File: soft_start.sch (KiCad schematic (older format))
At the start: 21 parts, among them J10 PWR, J8 MG950-9.5, J9 MG950-9.5, K5 Fujitsu_FTR-F1C, K6 Fujitsu_FTR-F1C, Q5 BC546, Q6 BC546, U5 NE555, U6 NE555

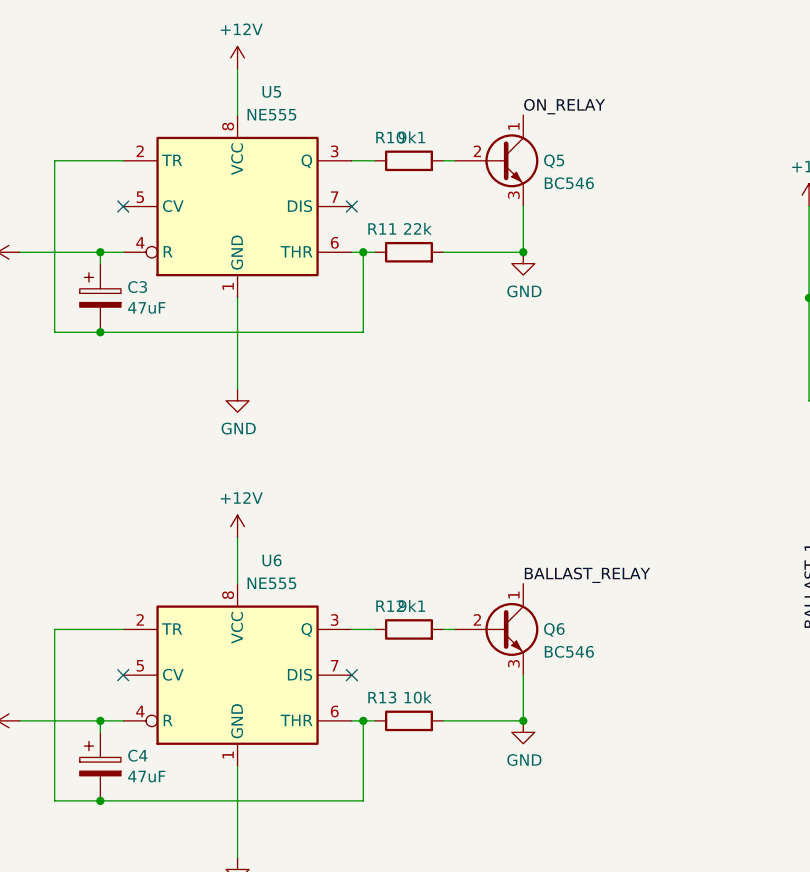
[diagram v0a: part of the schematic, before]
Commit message: Fix relay firing order in soft-start
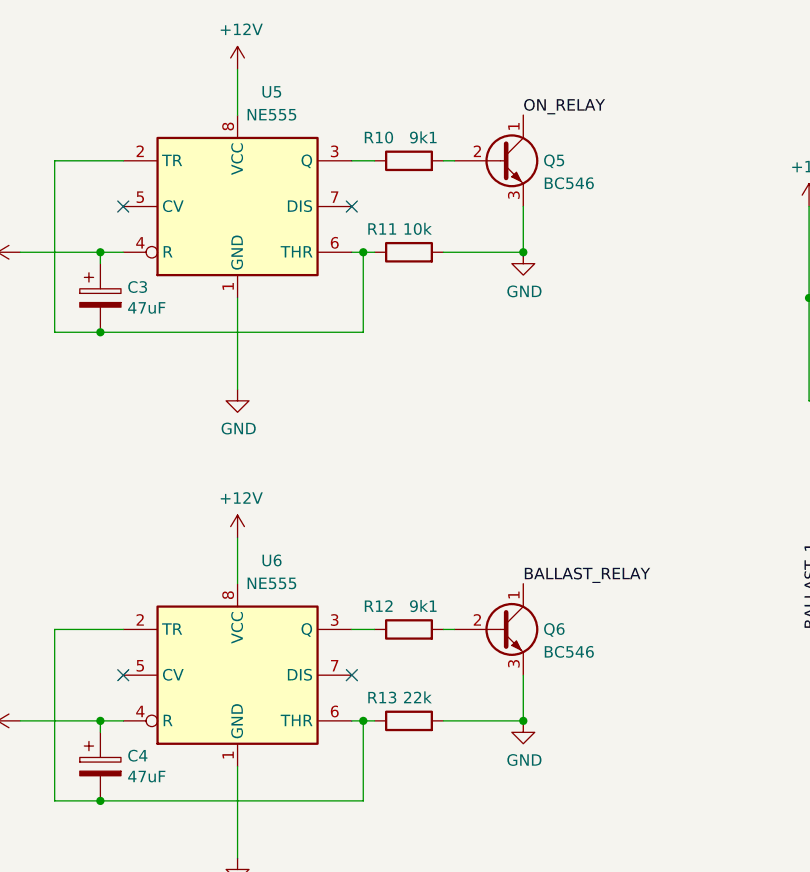
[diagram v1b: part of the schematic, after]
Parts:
- R11: value 22k -> 10k
- R13: value 10k -> 22k
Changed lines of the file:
@@
 AR Path="/5C1079DA/5C1080B8" Ref="R11"  Part="1"
 F 0 "R11" V 3150 1800 50  0000 L CNN
-F 1 "22k" V 3150 1650 50  0000 L CNN
+F 1 "10k" V 3150 1650 50  0000 L CNN
 F 2 "Resistor_THT:R_Axial_DIN0207_L6.3mm_D2.5mm_P2.54mm_Vertical" V 2980 1750 50  0001 C CNN
 F 3 "~" H 3050 1750 50  0001 C CNN
@@
 AR Path="/5C0DA8AE/5C10938F" Ref="R?"  Part="1"
 AR Path="/5C1079DA/5C10938F" Ref="R10"  Part="1"
-F 0 "R10" V 3150 1500 50  0000 R CNN
-F 1 "9k1" V 3150 1400 50  0000 R CNN
+F 0 "R10" V 3150 1550 50  0000 R CNN
+F 1 "9k1" V 3150 1350 50  0000 R CNN
 F 2 "Resistor_THT:R_Axial_DIN0207_L6.3mm_D2.5mm_P2.54mm_Vertical" V 2980 1350 50  0001 C CNN
 F 3 "~" H 3050 1350 50  0001 C CNN
@@
 AR Path="/5C1079DA/5C123CA7" Ref="R13"  Part="1"
 F 0 "R13" V 3150 3850 50  0000 L CNN
-F 1 "10k" V 3150 3700 50  0000 L CNN
+F 1 "22k" V 3150 3700 50  0000 L CNN
 F 2 "Resistor_THT:R_Axial_DIN0207_L6.3mm_D2.5mm_P2.54mm_Vertical" V 2980 3800 50  0001 C CNN
 F 3 "~" H 3050 3800 50  0001 C CNN
@@
 AR Path="/5C0DA8AE/5C123CB5" Ref="R?"  Part="1"
 AR Path="/5C1079DA/5C123CB5" Ref="R12"  Part="1"
-F 0 "R12" V 3150 3550 50  0000 R CNN
-F 1 "9k1" V 3150 3450 50  0000 R CNN
+F 0 "R12" V 3150 3600 50  0000 R CNN
+F 1 "9k1" V 3150 3400 50  0000 R CNN
 F 2 "Resistor_THT:R_Axial_DIN0207_L6.3mm_D2.5mm_P2.54mm_Vertical" V 2980 3400 50  0001 C CNN
 F 3 "~" H 3050 3400 50  0001 C CNN

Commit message: Final schematic version
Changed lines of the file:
@@
 EESchema Schematic File Version 4
 LIBS:isolation-transformer-cache
-EELAYER 26 0
+EELAYER 30 0
 EELAYER END
 $Descr A4 11693 8268
 encoding utf-8
-Sheet 3 3
+Sheet 2 3
 Title ""
 Date ""
@@
 	1    0    0    -1
 $EndComp
-Text Label 5550 3400 1    50   ~ 0
-PWR_1
-Text Label 6950 3400 1    50   ~ 0
-PWR_2
 Wire Wire Line
 	8550 1600 8000 1600
@@
 	1    0    0    -1
 $EndComp
-Text Label 8000 1500 0    50   ~ 0
-BALLAST_2
-Text Label 8000 1600 0    50   ~ 0
-PWR_2
 Wire Wire Line
 	8550 1300 8000 1300
@@
 	1    0    0    -1
 $EndComp
-Text Label 8000 1200 0    50   ~ 0
-PWR_1
-Text Label 8000 1300 0    50   ~ 0
-BALLAST_1
 Connection ~ 3550 1750
 $Comp
@@
 	1    0    0    -1
 $EndComp
-Text Label 6100 3400 1    50   ~ 0
-BALLAST_1
-Text Label 6800 3400 1    50   ~ 0
-BALLAST_2
 Text Label 6050 1850 1    50   ~ 0
 BALLAST_RELAY
@@
 Wire Wire Line
 	4850 2600 4850 2800
-Text Label 4850 3400 1    50   ~ 0
+Connection ~ 4850 2800
+Wire Wire Line
+	4850 2800 4850 3400
+Entry Wire Line
+	4850 3400 4950 3500
+Entry Wire Line
+	5550 3400 5650 3500
+Entry Wire Line
+	6100 3400 6200 3500
+Entry Wire Line
+	6800 3400 6900 3500
+Entry Wire Line
+	6950 3400 7050 3500
+Entry Wire Line
+	7900 1300 8000 1200
+Entry Wire Line
+	7900 1400 8000 1300
+Entry Wire Line
+	7900 1600 8000 1500
+Entry Wire Line
+	7900 1700 8000 1600
+Text HLabel 8000 1200 0    50   Input ~ 0
+PWR_1
+Text HLabel 8000 1300 0    50   Input ~ 0
 BALLAST_1
-Connection ~ 4850 2800
-Wire Wire Line
-	4850 2800 4850 3400
+Text HLabel 8000 1500 0    50   Input ~ 0
+BALLAST_2
+Text HLabel 8000 1600 0    50   Input ~ 0
+PWR_2
+Text HLabel 5550 3400 1    50   Input ~ 0
+PWR_1
+Text HLabel 6100 3400 1    50   Input ~ 0
+BALLAST_1
+Text HLabel 6800 3400 1    50   Input ~ 0
+BALLAST_2
+Text HLabel 6950 3400 1    50   Input ~ 0
+PWR_2
+Text HLabel 4850 3400 1    50   Input ~ 0
+BALLAST_1
+Wire Bus Line
+	4950 3500 7900 3500
+Wire Bus Line
+	7900 1300 7900 3500
 $EndSCHEMATC

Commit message: Actually used parts instead of generic ones
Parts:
- K5, K6: value Fujitsu_FTR-F1C -> FTR-K1CK012W; footprint Relay_THT:Relay_DPDT_Fujitsu_FTR-F1C -> CustomParts:Relay_SPDT_Fujitsu_FTR-K1C; symbol Relay:Fujitsu_FTR-F1C -> CustomParts:Fujitsu_FTR-K1C
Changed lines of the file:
@@
 	5450 2800 5550 2800
 Wire Wire Line
-	5550 2600 5550 2800
-Wire Wire Line
-	5450 2600 5550 2600
+	5550 2700 5550 2800
+Wire Wire Line
+	5450 2700 5550 2700
 $Comp
 L power:+12V #PWR?
@@
 	5550 2800 5550 3400
 $Comp
-L Relay:Fujitsu_FTR-F1C K?
+L CustomParts:Fujitsu_FTR-K1C K?
 U 1 1 5C1093A7
 P 5150 2600
@@
 AR Path="/5C1079DA/5C1093A7" Ref="K5"  Part="1"
 F 0 "K5" H 5150 3117 50  0000 C CNN
-F 1 "Fujitsu_FTR-F1C" H 5150 3026 50  0000 C CNN
-F 2 "Relay_THT:Relay_DPDT_Fujitsu_FTR-F1C" H 5100 2200 50  0001 C CNN
-F 3 "https://www.fujitsu.com/downloads/MICRO/fcai/relays/ftr-f1.pdf" H 5150 2850 50  0001 C CNN
+F 1 "FTR-K1CK012W" H 5150 3026 50  0000 C CNN
+F 2 "CustomParts:Relay_SPDT_Fujitsu_FTR-K1C" H 5100 2200 50  0001 C CNN
+F 3 "https://www.fujitsu.com/downloads/MICRO/fcai/relays/ftr-k1.pdf" H 5150 2850 50  0001 C CNN
 	1    5150 2600
 	1    0    0    -1
@@
 ON_RELAY
 NoConn ~ 5450 2500
-NoConn ~ 5450 2700
+NoConn ~ 5450 2600
 Wire Wire Line
 	6800 2800 6800 3400
@@
 	6700 2800 6800 2800
 Wire Wire Line
-	6800 2600 6800 2800
-Wire Wire Line
-	6700 2600 6800 2600
+	6800 2700 6800 2800
+Wire Wire Line
+	6700 2700 6800 2700
 $Comp
 L power:+12V #PWR?
@@
 $EndComp
 Wire Wire Line
-	6100 2800 6100 3400
-Wire Wire Line
-	6100 2600 6100 2800
-Connection ~ 6100 2800
-$Comp
-L Relay:Fujitsu_FTR-F1C K?
+	6100 2600 6100 2700
+Connection ~ 6100 2700
+$Comp
+L CustomParts:Fujitsu_FTR-K1C K?
 U 1 1 5C12A4C1
 P 6400 2600
@@
 AR Path="/5C1079DA/5C12A4C1" Ref="K6"  Part="1"
 F 0 "K6" H 6400 3117 50  0000 C CNN
-F 1 "Fujitsu_FTR-F1C" H 6400 3026 50  0000 C CNN
-F 2 "Relay_THT:Relay_DPDT_Fujitsu_FTR-F1C" H 6350 2200 50  0001 C CNN
-F 3 "https://www.fujitsu.com/downloads/MICRO/fcai/relays/ftr-f1.pdf" H 6400 2850 50  0001 C CNN
+F 1 "FTR-K1CK012W" H 6400 3026 50  0000 C CNN
+F 2 "CustomParts:Relay_SPDT_Fujitsu_FTR-K1C" H 6350 2200 50  0001 C CNN
+F 3 "https://www.fujitsu.com/downloads/MICRO/fcai/relays/ftr-k1.pdf" H 6400 2850 50  0001 C CNN
 	1    6400 2600
 	1    0    0    -1
@@
 BALLAST_RELAY
 NoConn ~ 6700 2500
-NoConn ~ 6700 2700
+NoConn ~ 6700 2600
 Connection ~ 6800 2800
 Wire Wire Line
@@
 Connection ~ 5550 2800
 Wire Wire Line
-	4850 2600 4850 2800
-Connection ~ 4850 2800
-Wire Wire Line
-	4850 2800 4850 3400
+	4850 2600 4850 2700
+Connection ~ 4850 2700
 Entry Wire Line
 	4850 3400 4950 3500
@@
 Text HLabel 4850 3400 1    50   Input ~ 0
 BALLAST_1
+Wire Wire Line
+	4850 2700 4850 3400
+Wire Wire Line
+	6100 2700 6100 3400
 Wire Bus Line
 	4950 3500 7900 3500
